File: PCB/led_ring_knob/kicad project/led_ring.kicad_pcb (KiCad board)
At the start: 2 copper layers, 28.4 x 24.4 mm, 70 parts, among them J1 DATA, J2 POW, U1 74HCT595PW, U2 74HCT595PW, U3 74HCT595PW, U4 74HCT595PW

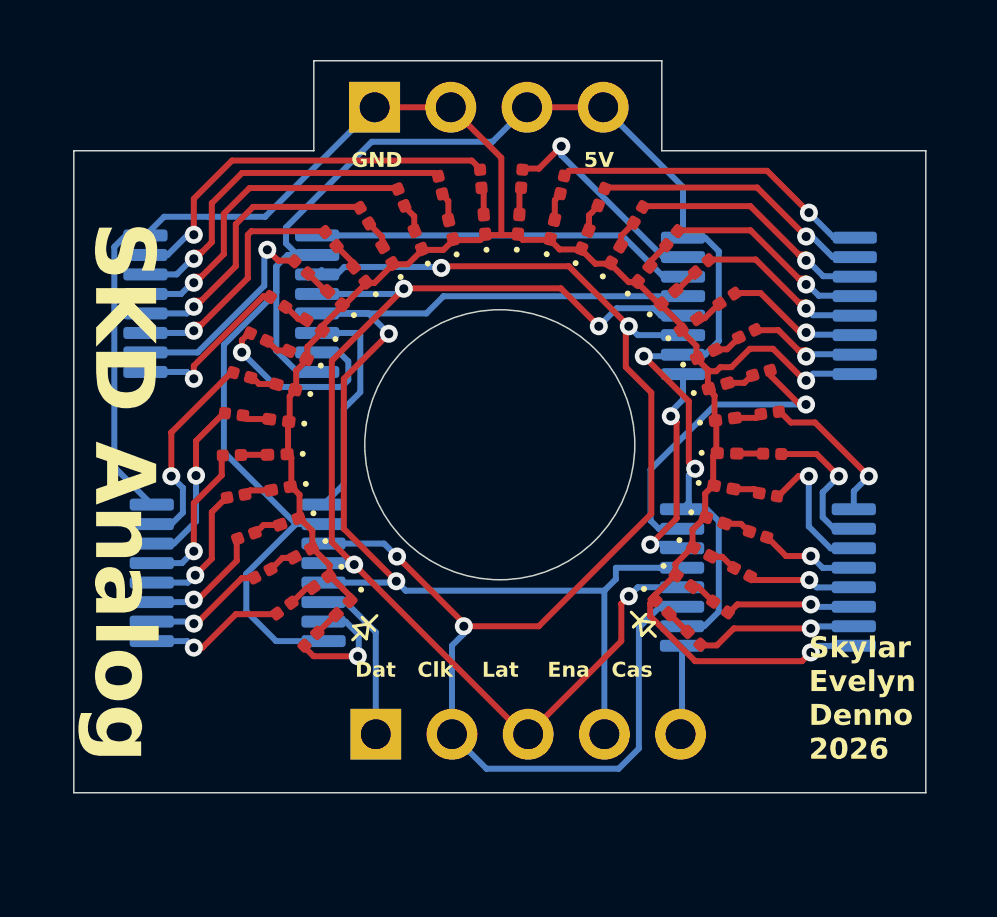
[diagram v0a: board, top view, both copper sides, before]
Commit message: led ring redesign
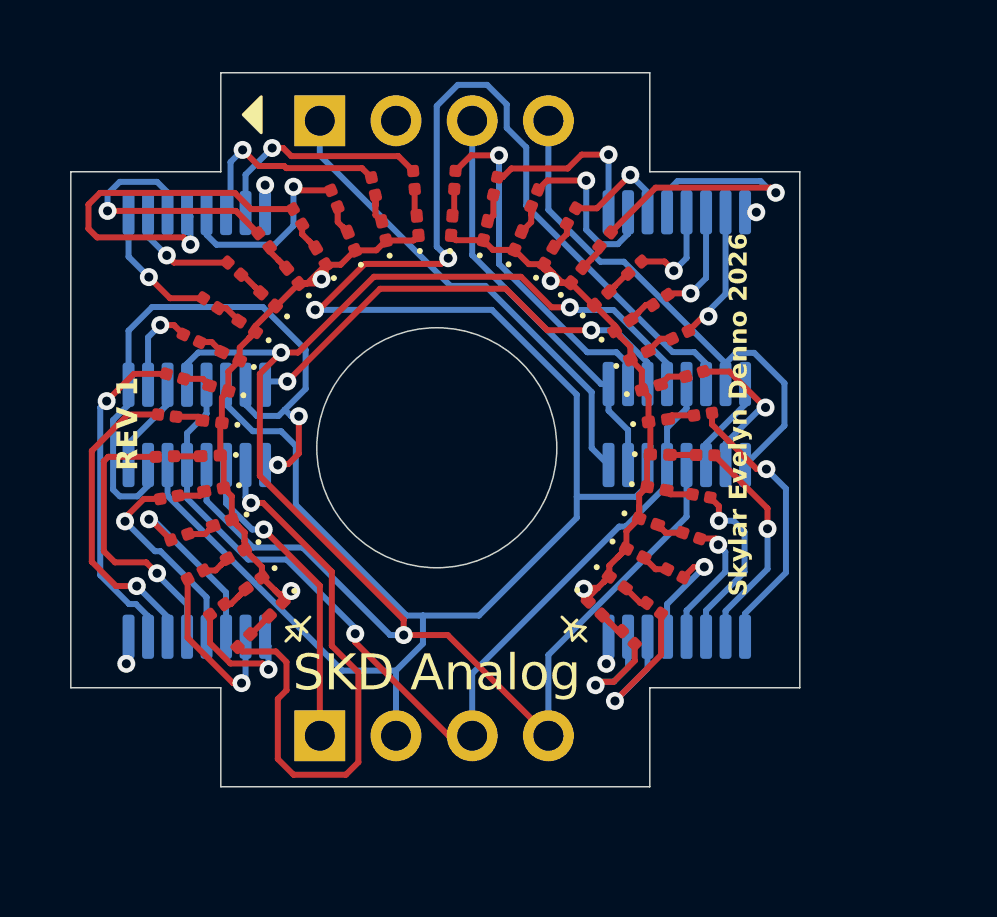
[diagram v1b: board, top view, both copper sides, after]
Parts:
- J1: footprint Connector_PinHeader_2.54mm:PinHeader_1x05_P2.54mm_Vertical -> Connector_PinHeader_2.54mm:PinHeader_1x04_P2.54mm_Vertical
- R1, R10, R11, R12, R13, R14, R15, R16, R17, R18, R19, R2, R20, R21, R22, R23, R24, R25, R26, R27, R28, R29, R3, R30, R31, R32, R4, R5, R6, R7, R8, R9: value 330 -> 470
- moved U4 3.16 mm to (136.1, 63.7), turned to 90 degrees
- moved U3 3.08 mm to (136.1, 55.3), turned to -90 degrees
- moved R27 2.23 mm to (137.0, 60.5), turned to 179 degrees
- moved D28 2.23 mm to (135.4, 61.7), turned to 80 degrees
- moved R19 2.23 mm to (131.4, 52.0), turned to -112 degrees
- moved D11 2.23 mm to (122.5, 55.4)
- moved R29 2.23 mm to (136.6, 63.2), turned to 161 degrees
- moved D23 2.23 mm to (134.3, 56.2), turned to 124 degrees
- moved R14 2.23 mm to (124.7, 52.0), turned to -68 degrees
- moved D21 2.23 mm to (132.8, 54.5)
- moved D25 2.23 mm to (135.3, 58.3), turned to 106 degrees
- moved R26 2.23 mm to (137.0, 59.2), turned to -172 degrees
- moved D1 2.23 mm to (122.7, 65.7)
- moved D32 2.23 mm to (133.4, 65.6), turned to 45 degrees
- moved R11 2.23 mm to (121.4, 54.3)
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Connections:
- J2 pad 1: Net-(D1-K) -> Net-(J2-Pin_1)
- U4 pad 9: Net-(J1-Pin_5) -> Net-(J2-Pin_1)
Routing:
- net Net-(D1-K): track 76.4 -> 45.7 mm, vias 2 -> 8
- net Net-(J1-Pin_2): track 50.5 -> 76.2 mm, vias 4 -> 2
- net Net-(J2-Pin_1): track 0.00 -> 16.1 mm
- net Net-(J1-Pin_4): track 42.1 -> 58.2 mm, vias 2 -> 3
- net Net-(U1-QA): track 4.02 -> 20.0 mm
- net Net-(J2-Pin_3): track 62.1 -> 53.3 mm
- net Net-(J1-Pin_3): track 40.7 -> 31.9 mm, vias 4 -> 1
- net Net-(U2-QH): track 13.3 -> 7.55 mm
- net Net-(U4-QA): track 10.7 -> 5.12 mm
- net Net-(U2-QG): track 12.1 -> 7.00 mm
- net Net-(J1-Pin_1): track 5.56 -> 10.5 mm, vias 0 -> 1
- net Net-(U3-QB): track 10.7 -> 5.94 mm
- net Net-(U1-QG): track 5.78 -> 10.4 mm
- net Net-(U1-QH'): track 7.62 -> 3.21 mm
- net Net-(U3-QD): track 8.12 -> 3.75 mm
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- added copper zone on In2.Cu, net Net-(D1-K)
- added copper zone on In1.Cu, net Net-(J2-Pin_3)
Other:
- board size 28.4 x 24.4 mm -> 24.3 x 23.8 mm
- copper layers 2 -> 4
- board text added: "REV 1"
- board text removed: "5V"
- board text removed: "Dat Clk Lat Ena Cas"
- board text removed: "GND"
